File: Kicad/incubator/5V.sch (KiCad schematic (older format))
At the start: 12 parts

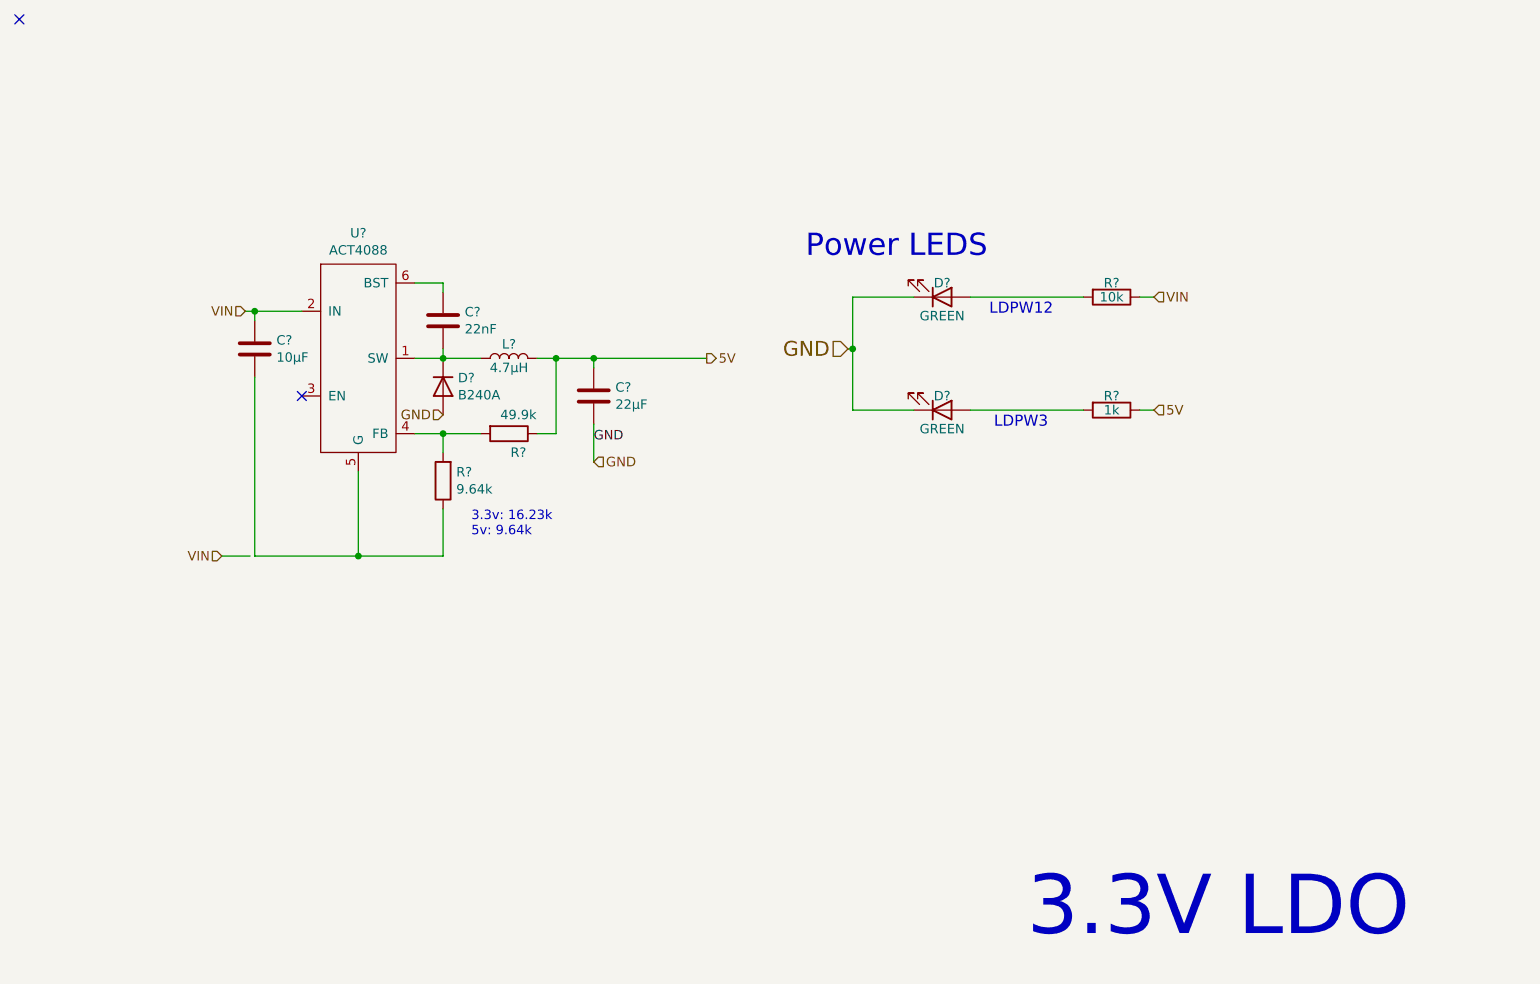
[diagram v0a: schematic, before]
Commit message: refactor:Step-down IC was changed
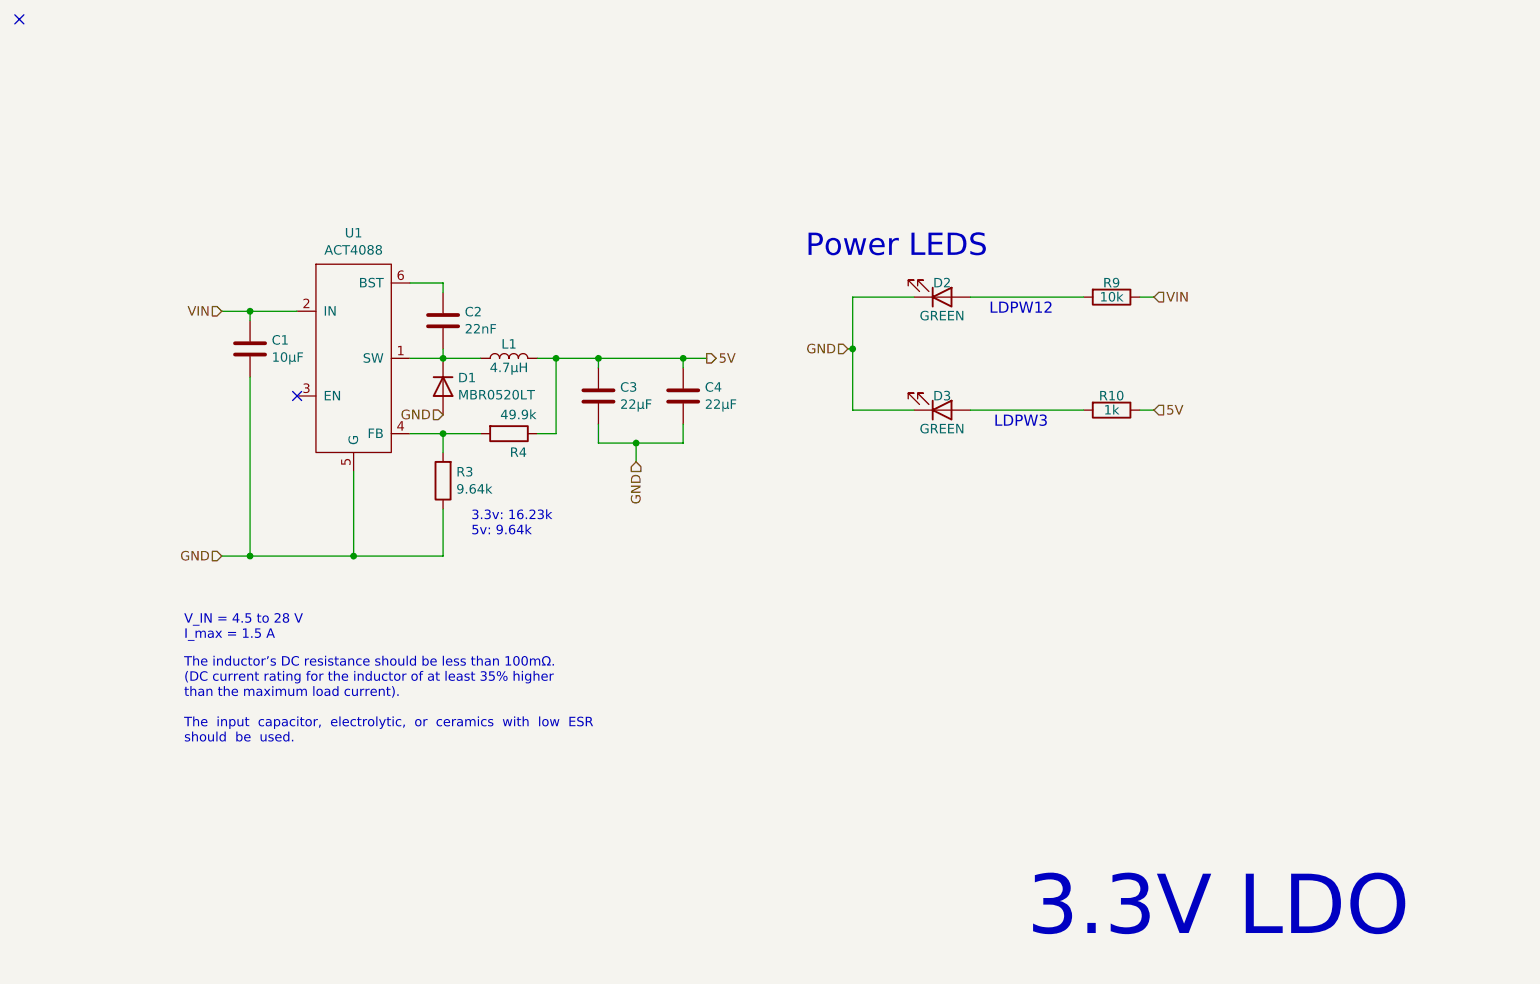
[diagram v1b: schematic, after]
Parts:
- added C4: 22µF, Capacitor_SMD:C_0805_2012Metric_Pad1.18x1.45mm_HandSolder, symbol Device:C
- C1, C2, C3: renamed from C?; footprint Capacitor_SMD:C_0805_2012Metric_Pad1.15x1.40mm_HandSolder -> Capacitor_SMD:C_0805_2012Metric_Pad1.18x1.45mm_HandSolder
- D1: renamed from D?; value B240A -> MBR0520LT
- L1: renamed from L?; footprint Inductor_SMD:L_0805_2012Metric_Pad1.15x1.40mm_HandSolder -> Inductor_SMD:L_Taiyo-Yuden_NR-40xx_HandSoldering
- R22, R23: footprint Resistor_SMD:R_0805_2012Metric_Pad1.15x1.40mm_HandSolder -> Resistor_SMD:R_0805_2012Metric_Pad1.20x1.40mm_HandSolder
- R3, R4: renamed from R?; footprint Resistor_SMD:R_0805_2012Metric_Pad1.15x1.40mm_HandSolder -> Resistor_SMD:R_0805_2012Metric_Pad1.20x1.40mm_HandSolder
- gave numbers to parts that had none: 3
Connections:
- wire segments 33 -> 39
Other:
- note added: "The inductor’s DC resistance should be less than 100mΩ. \n(DC current rating for the inductor of at least 35% higher \nthan the maximum load current).\n \nThe input capacitor, electrolytic, or ceramics with low ESR\nshould be used."
- note added: "V_IN = 4.5 to 28 V\nI_max = 1.5 A"
- moved on the sheet: C1, C3, U1
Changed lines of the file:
@@
 $Descr A4 11693 8268
 encoding utf-8
-Sheet 5 5
+Sheet 4 4
 Title ""
 Date ""
@@
 $EndDescr
 $Comp
-L ACT4088:ACT4088 U?
+L ACT4088:ACT4088 U1
 U 1 1 5E004CC9
-P 4325 4000
-F 0 "U?" H 4325 4715 50  0000 C CNN
-F 1 "ACT4088" H 4325 4624 50  0000 C CNN
-F 2 "Package_TO_SOT_SMD:SOT-23-6_Handsoldering" H 4375 4000 50  0001 C CNN
-F 3 "" H 4375 4000 50  0001 C CNN
-	1    4325 4000
-	1    0    0    -1
-$EndComp
-$Comp
-L Device:C C?
+P 4300 4000
+F 0 "U1" H 4300 4715 50  0000 C CNN
+F 1 "ACT4088" H 4300 4624 50  0000 C CNN
+F 2 "Package_TO_SOT_SMD:SOT-23-6_Handsoldering" H 4350 4000 50  0001 C CNN
+F 3 "" H 4350 4000 50  0001 C CNN
+	1    4300 4000
+	1    0    0    -1
+$EndComp
+$Comp
+L Device:C C2
 U 1 1 5E004CCF
 P 4775 3750
-F 0 "C?" H 4890 3796 50  0000 L CNN
+F 0 "C2" H 4890 3796 50  0000 L CNN
 F 1 "22nF" H 4890 3705 50  0000 L CNN
-F 2 "Capacitor_SMD:C_0805_2012Metric_Pad1.15x1.40mm_HandSolder" H 4813 3600 50  0001 C CNN
+F 2 "Capacitor_SMD:C_0805_2012Metric_Pad1.18x1.45mm_HandSolder" H 4813 3600 50  0001 C CNN
 F 3 "~" H 4775 3750 50  0001 C CNN
 	1    4775 3750
@@
 $EndComp
 $Comp
-L Device:R R?
+L Device:R R4
 U 1 1 5E004CDB
 P 5125 4350
-F 0 "R?" V 5225 4400 50  0000 C CNN
+F 0 "R4" V 5225 4400 50  0000 C CNN
 F 1 "49.9k" V 5025 4400 50  0000 C CNN
-F 2 "Resistor_SMD:R_0805_2012Metric_Pad1.15x1.40mm_HandSolder" V 5055 4350 50  0001 C CNN
+F 2 "Resistor_SMD:R_0805_2012Metric_Pad1.20x1.40mm_HandSolder" V 5055 4350 50  0001 C CNN
 F 3 "~" H 5125 4350 50  0001 C CNN
 	1    5125 4350
@@
 $EndComp
 $Comp
-L Device:R R?
+L Device:R R3
 U 1 1 5E004CE1
 P 4775 4600
-F 0 "R?" H 4705 4554 50  0000 R CNN
+F 0 "R3" H 4705 4554 50  0000 R CNN
 F 1 "9.64k" H 4705 4645 50  0000 R CNN
-F 2 "Resistor_SMD:R_0805_2012Metric_Pad1.15x1.40mm_HandSolder" V 4705 4600 50  0001 C CNN
+F 2 "Resistor_SMD:R_0805_2012Metric_Pad1.20x1.40mm_HandSolder" V 4705 4600 50  0001 C CNN
 F 3 "~" H 4775 4600 50  0001 C CNN
 	1    4775 4600
 	-1   0    0    1
 $EndComp
-Text HLabel 3725 3700 0    50   Input ~ 0
+Text HLabel 3600 3700 0    50   Input ~ 0
 VIN
-Wire Wire Line
-	3725 3700 3775 3700
-Wire Wire Line
-	4625 4350 4775 4350
 Wire Wire Line
 	4775 4450 4775 4350
@@
 	5375 4350 5375 3950
 Wire Wire Line
-	5375 3950 5275 3950
-Wire Wire Line
 	4975 3950 4775 3950
 Wire Wire Line
@@
 Connection ~ 4775 3950
 Wire Wire Line
-	4775 3950 4625 3950
-Wire Wire Line
-	4625 3550 4775 3550
-Wire Wire Line
 	4775 3550 4775 3600
-Wire Wire Line
-	5375 3950 5575 3950
-Wire Wire Line
-	5575 3950 5575 4000
-Connection ~ 5375 3950
 Text HLabel 6175 3950 2    50   Output ~ 0
 5V
-Connection ~ 5575 3950
-$Comp
-L Device:C C?
-U 1 1 5E004D0F
-P 3775 3900
-F 0 "C?" H 3890 3946 50  0000 L CNN
-F 1 "10µF" H 3890 3855 50  0000 L CNN
-F 2 "Capacitor_SMD:C_0805_2012Metric_Pad1.15x1.40mm_HandSolder" H 3813 3750 50  0001 C CNN
-F 3 "~" H 3775 3900 50  0001 C CNN
-	1    3775 3900
-	1    0    0    -1
-$EndComp
-Wire Wire Line
-	3775 3750 3775 3700
 Text Notes 4925 4900 0    50   ~ 0
 3.3v: 16.23k\n5v: 9.64k
-Wire Wire Line
-	5575 3950 6175 3950
-$Comp
-L Device:D D?
+$Comp
+L Device:D D1
 U 1 1 5E004D28
 P 4775 4100
-F 0 "D?" V 4729 4179 50  0000 L CNN
-F 1 "B240A" V 4820 4179 50  0000 L CNN
+F 0 "D1" V 4729 4179 50  0000 L CNN
+F 1 "MBR0520LT" V 4820 4179 50  0000 L CNN
 F 2 "Diode_SMD:D_SOD-123" H 4775 4100 50  0001 C CNN
 F 3 "~" H 4775 4100 50  0001 C CNN
@@
 	0    1    1    0
 $EndComp
-NoConn ~ 4025 4150
+NoConn ~ 4000 4150
 Text Notes 6700 3425 0    118  ~ 0
 Power LEDS
@@
 AR Path="/5E1D0FCF" Ref="R?"  Part="1"
 AR Path="/5E0005EE/5E1D0FCF" Ref="R22"  Part="1"
-AR Path="/614262A1/5E1D0FCF" Ref="R?"  Part="1"
-F 0 "R?" V 8250 3625 50  0000 C CNN
+AR Path="/614262A1/5E1D0FCF" Ref="R9"  Part="1"
+F 0 "R9" V 8250 3625 50  0000 C CNN
 F 1 "10k" V 8325 3625 50  0000 C CNN
-F 2 "Resistor_SMD:R_0805_2012Metric_Pad1.15x1.40mm_HandSolder" V 8255 3625 50  0001 C CNN
+F 2 "Resistor_SMD:R_0805_2012Metric_Pad1.20x1.40mm_HandSolder" V 8255 3625 50  0001 C CNN
 F 3 "~" H 8325 3625 50  0001 C CNN
 	1    8325 3625
@@
 AR Path="/5E1D0FDF" Ref="R?"  Part="1"
 AR Path="/5E0005EE/5E1D0FDF" Ref="R23"  Part="1"
-AR Path="/614262A1/5E1D0FDF" Ref="R?"  Part="1"
-F 0 "R?" V 8250 4225 50  0000 C CNN
+AR Path="/614262A1/5E1D0FDF" Ref="R10"  Part="1"
+F 0 "R10" V 8250 4225 50  0000 C CNN
 F 1 "1k" V 8325 4225 50  0000 C CNN
-F 2 "Resistor_SMD:R_0805_2012Metric_Pad1.15x1.40mm_HandSolder" V 8255 4225 50  0001 C CNN
+F 2 "Resistor_SMD:R_0805_2012Metric_Pad1.20x1.40mm_HandSolder" V 8255 4225 50  0001 C CNN
 F 3 "~" H 8325 4225 50  0001 C CNN
 	1    8325 4225
@@
 Wire Wire Line
 	7575 3625 8175 3625
-Text Label 5575 4400 0    50   ~ 0
-GND
-$Comp
-L Device:C C?
-U 1 1 5E004CFD
-P 5575 4150
-F 0 "C?" H 5690 4196 50  0000 L CNN
-F 1 "22µF" H 5690 4105 50  0000 L CNN
-F 2 "Capacitor_SMD:C_0805_2012Metric_Pad1.15x1.40mm_HandSolder" H 5613 4000 50  0001 C CNN
-F 3 "~" H 5575 4150 50  0001 C CNN
-	1    5575 4150
-	1    0    0    -1
-$EndComp
-Wire Wire Line
-	3775 4050 3775 5000
-Wire Wire Line
-	3775 5000 4325 5000
-Wire Wire Line
-	4325 4550 4325 5000
-Wire Wire Line
-	4325 5000 4775 5000
 Wire Wire Line
 	4775 4750 4775 5000
-Connection ~ 4325 5000
 Text HLabel 4775 4250 0    51   Input ~ 0
 GND
-Text HLabel 6925 3900 0    79   Input ~ 0
+Text HLabel 6925 3900 0    50   Input ~ 0
 GND
 Wire Wire Line
@@
 Text HLabel 8550 4225 2    51   Input ~ 0
 5V
-Text HLabel 5575 4500 2    51   Input ~ 0
-GND
-Wire Wire Line
-	5575 4300 5575 4500
-Wire Wire Line
-	4025 3700 3775 3700
-Connection ~ 3775 3700
-$Comp
-L Device:LED D?
+Text HLabel 5800 4500 3    51   Input ~ 0
+GND
+$Comp
+L Device:LED D2
 U 1 1 5E883301
 P 7425 3625
-F 0 "D?" H 7425 3550 50  0000 C CNN
+F 0 "D2" H 7425 3550 50  0000 C CNN
 F 1 "GREEN" H 7425 3725 50  0000 C CNN
 F 2 "LED_SMD:LED_0805_2012Metric_Pad1.15x1.40mm_HandSolder" H 7425 3625 50  0001 C CNN
@@
 $EndComp
 $Comp
-L Device:LED D?
+L Device:LED D3
 U 1 1 5E886D2D
 P 7425 4225
-F 0 "D?" H 7425 4150 50  0000 C CNN
+F 0 "D3" H 7425 4150 50  0000 C CNN
 F 1 "GREEN" H 7425 4325 50  0000 C CNN
 F 2 "LED_SMD:LED_0805_2012Metric_Pad1.15x1.40mm_HandSolder" H 7425 4225 50  0001 C CNN
@@
 3.3V LDO
 $Comp
-L Device:L L?
+L Device:L L1
 U 1 1 5E004CD5
 P 5125 3950
-F 0 "L?" V 5200 3950 50  0000 C CNN
+F 0 "L1" V 5200 3950 50  0000 C CNN
 F 1 "4.7µH" V 5075 3950 50  0000 C CNN
-F 2 "Inductor_SMD:L_0805_2012Metric_Pad1.15x1.40mm_HandSolder" H 5125 3950 50  0001 C CNN
+F 2 "Inductor_SMD:L_Taiyo-Yuden_NR-40xx_HandSoldering" H 5125 3950 50  0001 C CNN
 F 3 "~" H 5125 3950 50  0001 C CNN
 	1    5125 3950
@@
 NoConn ~ 2525 2150
 Text HLabel 3600 5000 0    50   Input ~ 0
-VIN
-Wire Wire Line
-	3600 5000 3750 5000
+GND
+Wire Wire Line
+	4300 4550 4300 5000
+Wire Wire Line
+	4300 5000 4775 5000
+$Comp
+L Device:C C1
+U 1 1 5E004D0F
+P 3750 3900
+F 0 "C1" H 3865 3946 50  0000 L CNN
+F 1 "10µF" H 3865 3855 50  0000 L CNN
+F 2 "Capacitor_SMD:C_0805_2012Metric_Pad1.18x1.45mm_HandSolder" H 3788 3750 50  0001 C CNN
+F 3 "~" H 3750 3900 50  0001 C CNN
+	1    3750 3900
+	1    0    0    -1
+$EndComp
+Wire Wire Line
+	4300 5000 3750 5000
+Connection ~ 4300 5000
+Wire Wire Line
+	3750 4050 3750 5000
+Connection ~ 3750 5000
+Wire Wire Line
+	3750 5000 3600 5000
+Wire Wire Line
+	4000 3700 3750 3700
+Wire Wire Line
+	3750 3750 3750 3700
+Connection ~ 3750 3700
+Wire Wire Line
+	3750 3700 3600 3700
+Wire Wire Line
+	4600 3550 4775 3550
+Wire Wire Line
+	4600 3950 4775 3950
+Wire Wire Line
+	4600 4350 4775 4350
+Text Notes 3400 6000 0    50   ~ 0
+The inductor’s DC resistance should be less than 100mΩ. \n(DC current rating for the inductor of at least 35% higher \nthan the maximum load current).\n \nThe  input  capacitor,  electrolytic,  or  ceramics  with  low  ESR\nshould  be  used.
+Text Notes 3400 5450 0    50   ~ 0
+V_IN = 4.5 to 28 V\nI_max = 1.5 A
+$Comp
+L Device:C C4
+U 1 1 6146FF2C
+P 6050 4150
+F 0 "C4" H 6165 4196 50  0000 L CNN
+F 1 "22µF" H 6165 4105 50  0000 L CNN
+F 2 "Capacitor_SMD:C_0805_2012Metric_Pad1.18x1.45mm_HandSolder" H 6088 4000 50  0001 C CNN
+F 3 "~" H 6050 4150 50  0001 C CNN
+	1    6050 4150
+	1    0    0    -1
+$EndComp
+Wire Wire Line
+	5600 4300 5600 4400
+Wire Wire Line
+	5600 4400 5800 4400
+Wire Wire Line
+	6050 4400 6050 4300
+Wire Wire Line
+	6050 4000 6050 3950
+Wire Wire Line
+	6050 3950 6175 3950
+Wire Wire Line
+	5800 4500 5800 4400
+Connection ~ 5800 4400
+Wire Wire Line
+	5800 4400 6050 4400
+$Comp
+L Device:C C3
+U 1 1 5E004CFD
+P 5600 4150
+F 0 "C3" H 5715 4196 50  0000 L CNN
+F 1 "22µF" H 5715 4105 50  0000 L CNN
+F 2 "Capacitor_SMD:C_0805_2012Metric_Pad1.18x1.45mm_HandSolder" H 5638 4000 50  0001 C CNN
+F 3 "~" H 5600 4150 50  0001 C CNN
+	1    5600 4150
+	1    0    0    -1
+$EndComp
+Wire Wire Line
+	5600 4000 5600 3950
+Wire Wire Line
+	5600 3950 6050 3950
+Connection ~ 6050 3950
+Wire Wire Line
+	5275 3950 5375 3950
+Connection ~ 5600 3950
+Connection ~ 5375 3950
+Wire Wire Line
+	5375 3950 5600 3950
 $EndSCHEMATC
